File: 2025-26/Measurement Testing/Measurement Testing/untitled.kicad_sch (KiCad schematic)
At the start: 8 parts, among them U1 LMR51420XDDCR

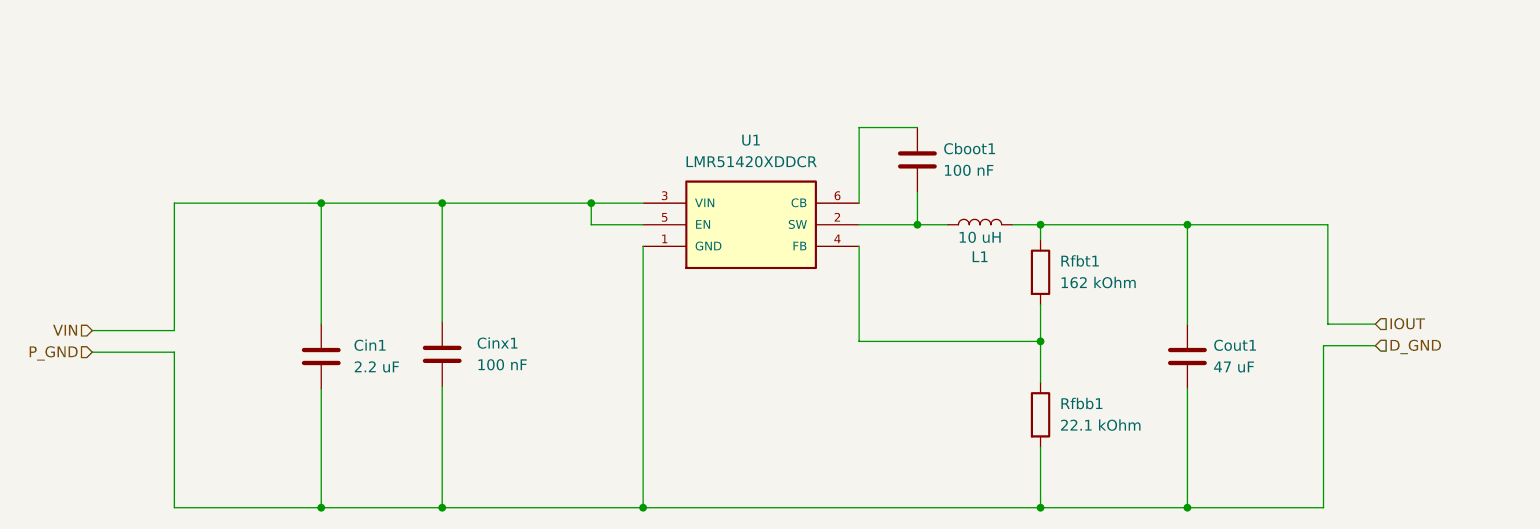
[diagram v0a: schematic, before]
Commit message: Updating PSU
Updated the 5V PSU Schematic with the correct components
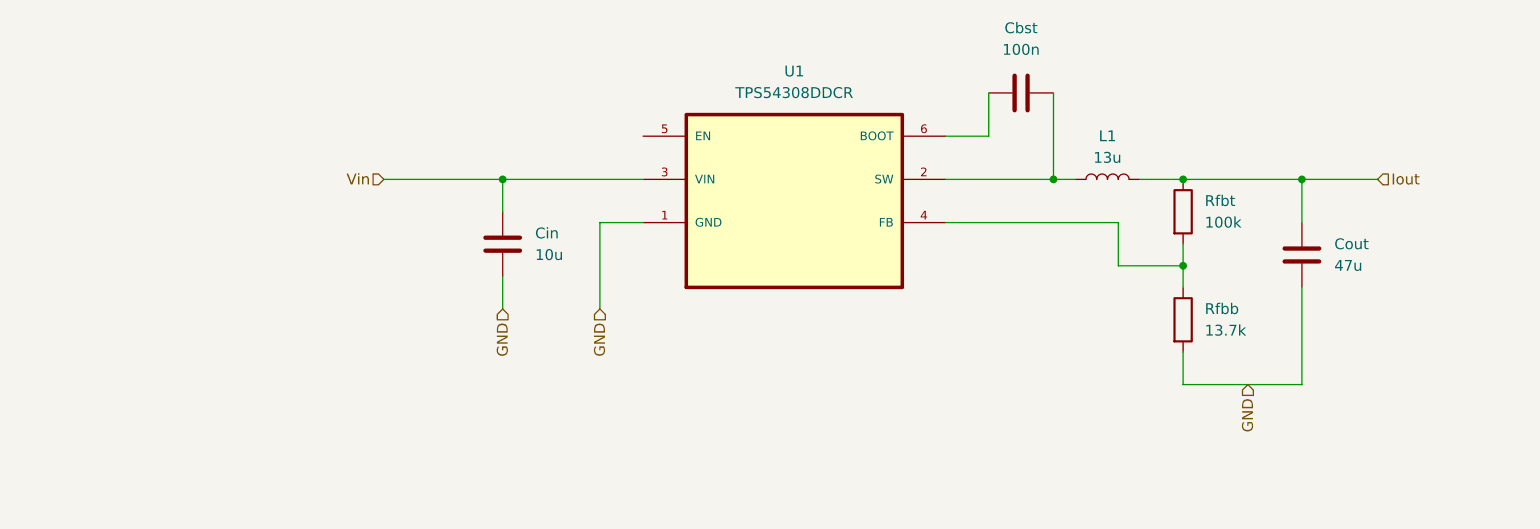
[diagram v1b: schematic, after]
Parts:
- removed Cboot1: 100 nF, Capacitor_SMD:C_0402_1005Metric_Pad0.74x0.62mm_HandSolder, symbol Device:C
- removed Cin1: 2.2 uF, Capacitor_SMD:C_1206_3216Metric_Pad1.33x1.80mm_HandSolder, symbol Device:C
- removed Cinx1: 100 nF, Capacitor_SMD:C_0603_1608Metric, symbol Device:C
- removed Cout1: 47 uF, Capacitor_SMD:C_1210_3225Metric_Pad1.33x2.70mm_HandSolder, symbol Device:C
- removed Rfbb1: 22.1 kOhm, Resistor_SMD:R_0402_1005Metric_Pad0.72x0.64mm_HandSolder, symbol Device:R
- removed Rfbt1: 162 kOhm, Resistor_SMD:R_0402_1005Metric_Pad0.72x0.64mm_HandSolder, symbol Device:R
- removed U1: LMR51420XDDCR, Library:SOT23_DDC_TEX, symbol LMR51420XDDCR:LMR51420XDDCR
- added Cbst: 100n, Capacitor_SMD:C_1206_3216Metric, symbol Device:C
- added Cin: 10u, Capacitor_SMD:C_1206_3216Metric, symbol Device:C
- added Cout: 47u, Capacitor_SMD:C_0805_2012Metric, symbol Device:C
- added Rfbb: 13.7k, Resistor_SMD:R_0402_1005Metric_Pad0.72x0.64mm_HandSolder, symbol Device:R
- added Rfbt: 100k, Resistor_SMD:R_0402_1005Metric_Pad0.72x0.64mm_HandSolder, symbol Device:R
- added U1: TPS54308DDCR, TPS54308DDCR:SOT95P280X110-6N, symbol TPS54308DDCR:TPS54308DDCR
- L1: value 10 uH -> 13u; footprint Library:IND_TAIYO_NRS8030_TAY -> Inductor_SMD:L_Wuerth_WE-PDF
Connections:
- net at L1.1: now also Cbst.2, U1.2 (SW)
- net IOUT renamed Iout
- net Iout: now also Cout.1, Rfbt.1
- new net: Cbst.1, U1.6 (BOOT)
- new net: Rfbb.1, Rfbt.2, U1.4 (FB)
- new net GND: Cin.2, Cout.2, Rfbb.2, U1.1 (GND)
- new net Vin: Cin.1, U1.3 (VIN)

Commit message: fixed all footprints
also added the pad areas for the alligator clips
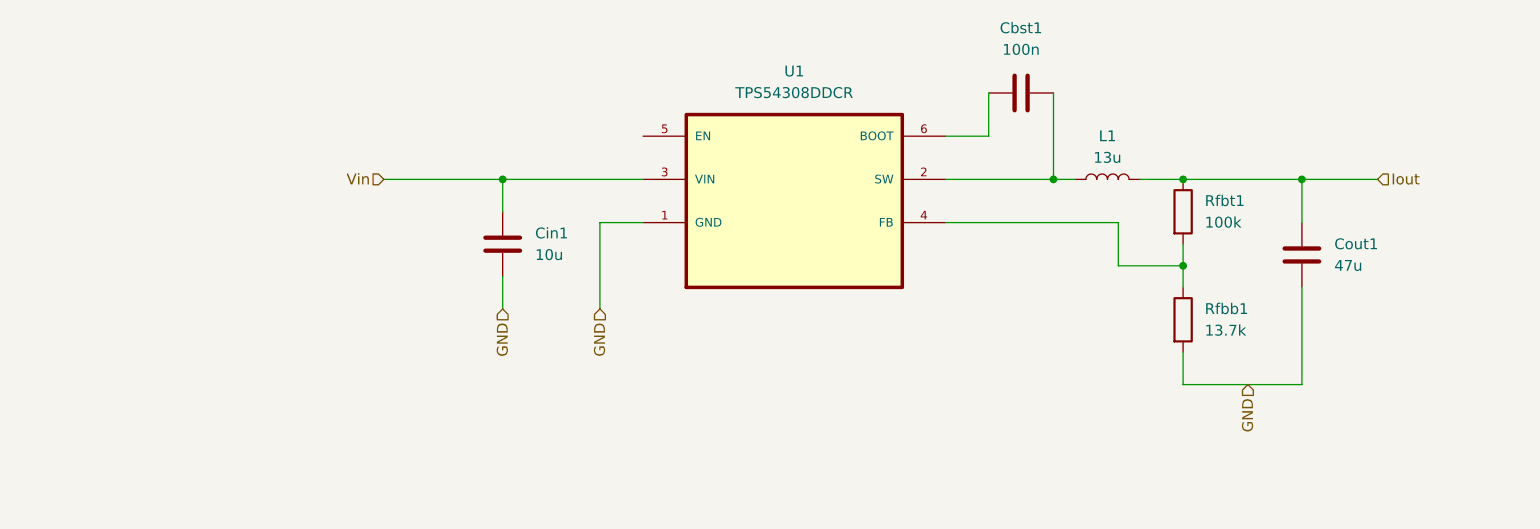
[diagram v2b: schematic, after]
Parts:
- Cbst1: renamed from Cbst; footprint Capacitor_SMD:C_1206_3216Metric -> Capacitor_SMD:C_0402_1005Metric
- U1: footprint TPS54308DDCR:SOT95P280X110-6N -> Package_TO_SOT_SMD:SOT-23-6
- renumbered Cin to Cin1, Cout to Cout1, Rfbb to Rfbb1, Rfbt to Rfbt1

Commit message: fixed schem issues, reset my board bc it did not have a gnd plane
yahooooooooooo
fixed the labels to be global, fixed a missing ground on schem.
added a ground plane to the board, removed traces (to redo with the ground plane)
- Rowan :3
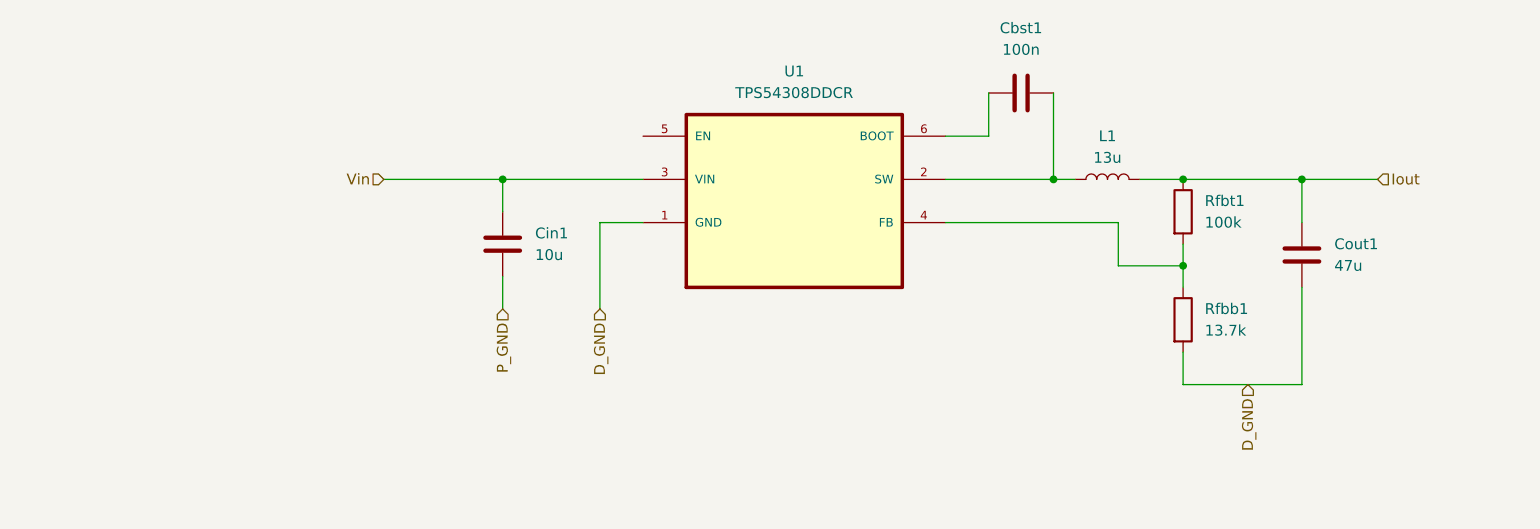
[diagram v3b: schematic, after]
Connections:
- net GND renamed D_GND
- net D_GND: no longer Cin1.2
- new net P_GND: Cin1.2
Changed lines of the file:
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@@
 		)
 	)
-	(hierarchical_label "GND"
+	(hierarchical_label "D_GND"
 		(shape input)
 		(at 207.01 101.6 270)
@@
 		)
 	)
-	(hierarchical_label "GND"
+	(hierarchical_label "P_GND"
 		(shape input)
 		(at 119.38 92.71 270)
@@
 		)
 	)
-	(hierarchical_label "GND"
+	(hierarchical_label "D_GND"
 		(shape input)
 		(at 130.81 92.71 270)

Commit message: started adding vias but then i realized idk what im doing
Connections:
- net Iout: no longer Cout1.1, L1.2, Rfbt1.1
- new net 5V: Cout1.1, L1.2, Rfbt1.1
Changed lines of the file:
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@@
 	(wire
 		(pts
-			(xy 213.36 77.47) (xy 222.25 77.47)
+			(xy 213.36 77.47) (xy 227.33 77.47)
 		)
 		(stroke
@@
 		)
 	)
+	(global_label "5V"
+		(shape input)
+		(at 227.33 77.47 0)
+		(fields_autoplaced yes)
+		(effects
+			(font
+				(size 1.27 1.27)
+			)
+			(justify left)
+		)
+		(property "Intersheetrefs" "${INTERSHEET_REFS}"
+			(at 232.6133 77.47 0)
+			(effects
+				(font
+					(size 1.27 1.27)
+				)
+				(justify left)
+				(hide yes)
+			)
+		)
+	)
 	(hierarchical_label "Vin"
 		(shape input)
@@
 	(hierarchical_label "Iout"
 		(shape input)
-		(at 222.25 77.47 0)
+		(at 232.41 66.04 0)
 		(effects
 			(font
